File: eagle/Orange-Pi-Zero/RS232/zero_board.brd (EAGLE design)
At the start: 49.3 x 49 mm, 17 parts, among them J1 RS-232, U1 MAX3232CDR

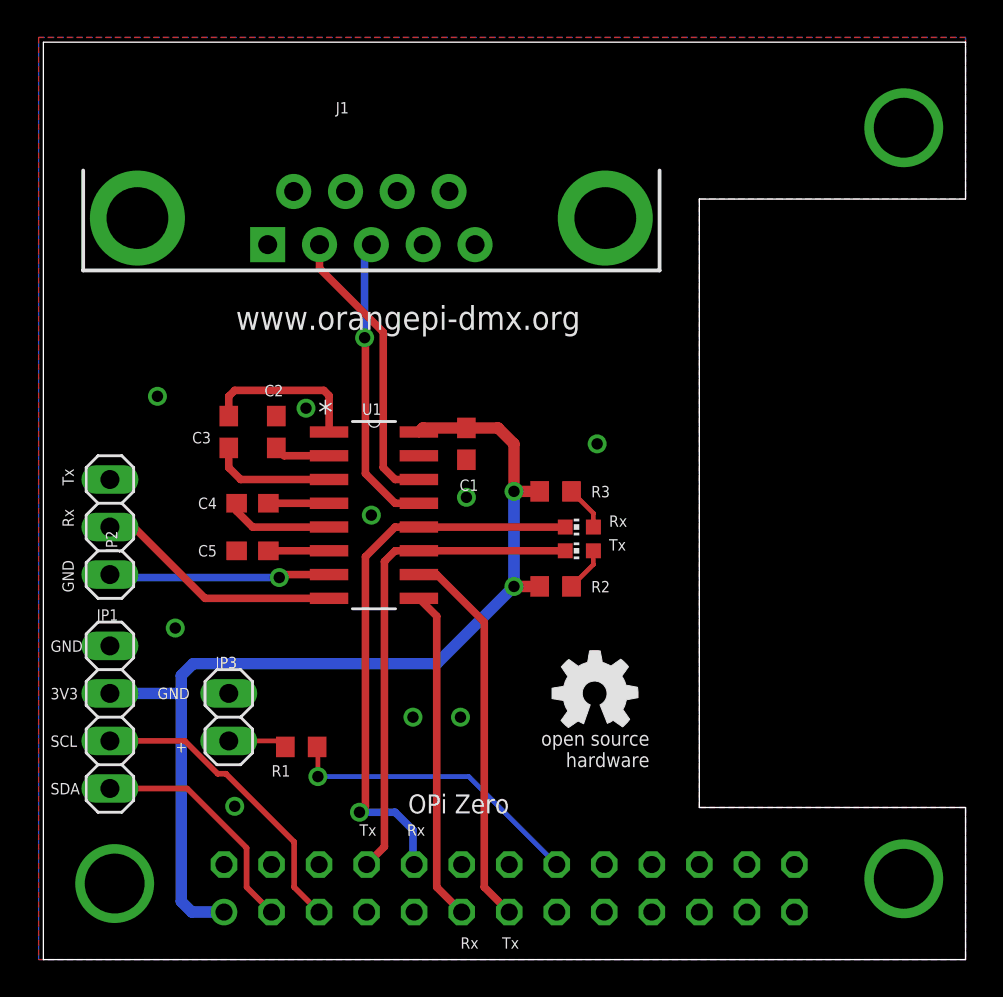
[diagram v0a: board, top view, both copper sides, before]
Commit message: Added RGB Panel board.
*. Updated RS232 board
*. Minor fix in BOM fort the 8x pixel board
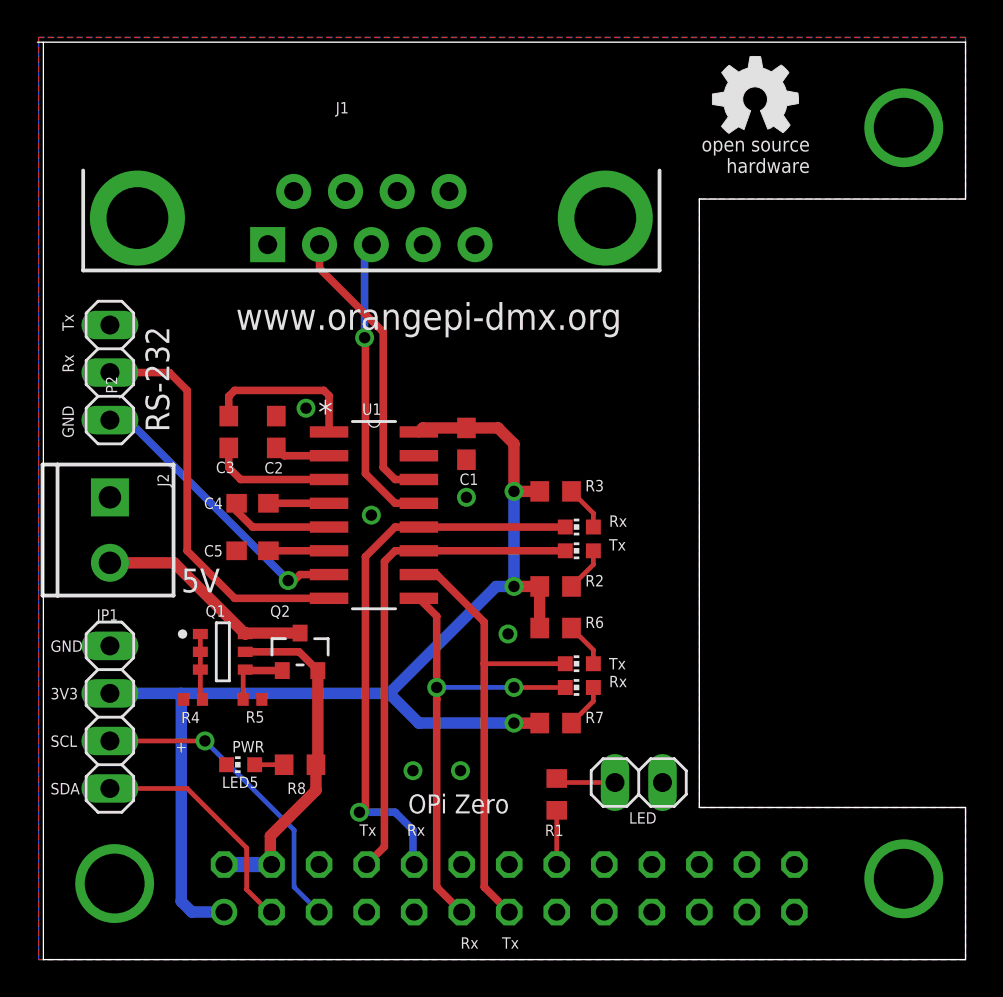
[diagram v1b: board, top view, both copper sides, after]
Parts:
- added J2: 5V, SparkFun-Connectors:SCREWTERMINAL-3.5MM-2
- added LED3, LED4: Green, led:CHIP-LED0603
- added LED5: PWR, led:CHIP-LED0603
- added Q1: DIODES_DMMT5401-7-FDIODES_DMMT5401-7-F_0_0, Diodes - DMMT5401-7-F:DIODES_DMMT5401-7-F_0
- added Q2: DIODES_INC._DMG2305UX-13DIODES_INC._DMG2305UX-13_0_0, Diodes Inc. - DMG2305UX-13:DIODES_INC._DMG2305UX-13_0
- added R4: 10K, rcl:R0402
- added R5: 47K, rcl:R0402
- added R6, R7, R8: 1K, resistor:R0603
- moved GOLD_ORB_SM1 32.9 mm to (38.3, 44.5)
- moved JP3 22.2 mm to (32.1, 7.94), turned to 180 degrees
- moved R1 13.9 mm to (27.7, 7.30), turned to 270 degrees
- moved JP2 8.25 mm to (3.81, 29.8)
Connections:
- new net 5V: Q1.5, Q2.2, R8.1, SV1.2, SV1.4
- new net N$10: Q1.1, Q1.2, Q1.3, R4.2
- new net N$11: J2.2, Q1.6, Q2.3
- new net N$12: Q1.4, Q2.1, R5.2
- new net N$13: LED3.A, R6.2
- new net N$14: LED4.A, R7.2
- new net N$15: LED5.A, R8.2
- net 3V3: now also R6.1, R7.1
- net GND: now also J2.1, LED5.C, R4.1, R5.1
- net RX_2: now also LED4.C
- net TX_2: now also LED3.C
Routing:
- net 5V: track 0.00 -> 18.3 mm
- net N$4: track 16.3 -> 2.90 mm, vias 1 -> 0
- net N$11: track 0.00 -> 11.8 mm
- net 3V3: track 54.0 -> 64.4 mm, vias 2 -> 3
- net R2IN: track 13.3 -> 21.7 mm
- net RX_2: track 17.7 -> 24.6 mm, vias 0 -> 2
- net TX_2: track 20.6 -> 24.9 mm
- net N$12: track 0.00 -> 3.63 mm
- net T2OUT: track 11.8 -> 15.4 mm
- net N$10: track 0.00 -> 3.54 mm
- net N$13: track 0.00 -> 2.39 mm
- net N$14: track 0.00 -> 2.39 mm
- net N$15: track 0.00 -> 1.57 mm
- net I2C_SCL: track 16.4 -> 16.7 mm, vias 0 -> 1
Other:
- board size 49.3 x 49 mm -> 49.6 x 49 mm
